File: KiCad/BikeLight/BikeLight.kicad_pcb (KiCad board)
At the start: 2 copper layers, 170.5 x 50 mm, 64 parts, among them J1 Conn-01x02_P2.5mm_S2B-XH-A-BK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, J2 Conn-01x02_P2.5mm_S2B-XH-A-BK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, J3 GT-USB-7051A, J4 Conn-01x02_P2.5mm_S2B-XH-A-BK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, J5 Conn-01x02_P2.5mm_S2B-XH-A-BK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, J6 Conn_01x05, Q1 AO3401A, Q2 AO3400A, Q3 BC847BDW1, SW2 SW_PB_B3F-4055, SW3 K2-1102AQ-H4CW-01, U1 TP4056-42-ESOP8, U2 MPU-6050, U3 MAX17048, U4 MCP1826S-33, U5 RFID-RC522, U6 MT3608, U8 HT-CT62

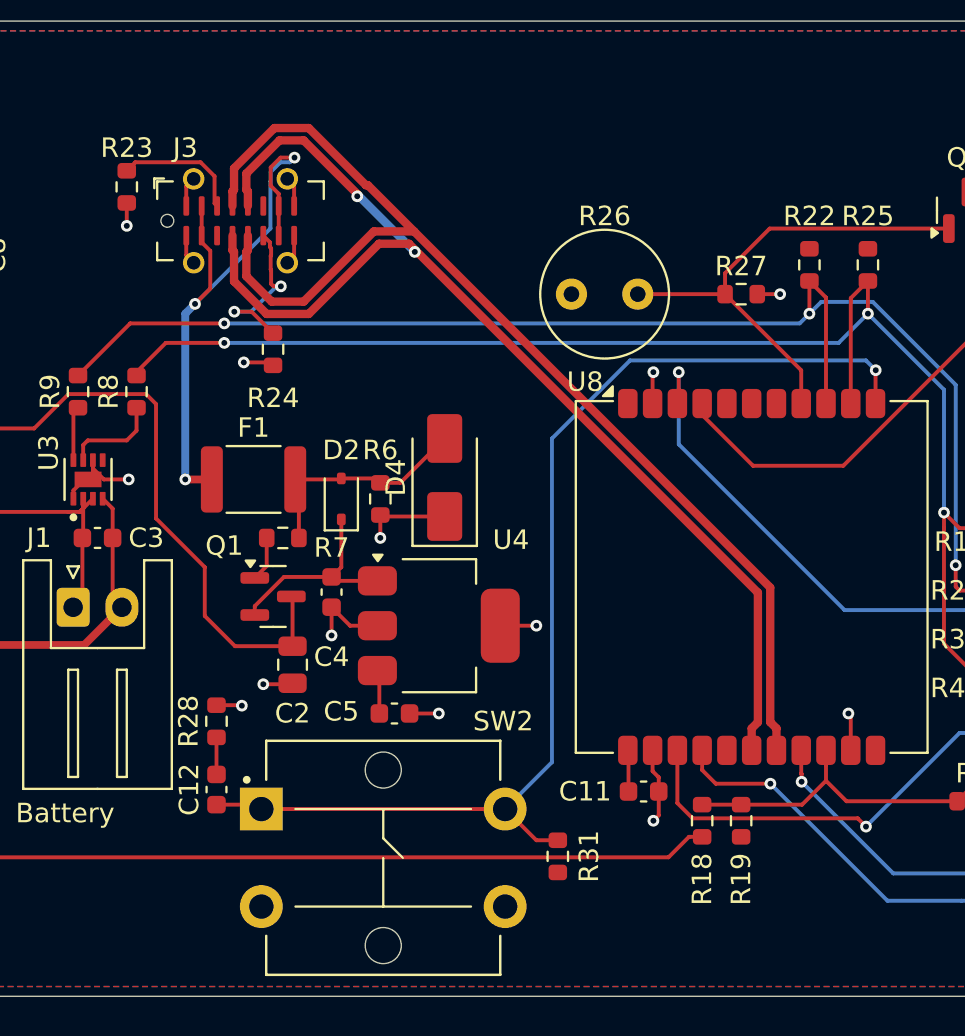
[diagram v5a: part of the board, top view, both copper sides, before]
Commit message: Changed and updated 3D models of devices
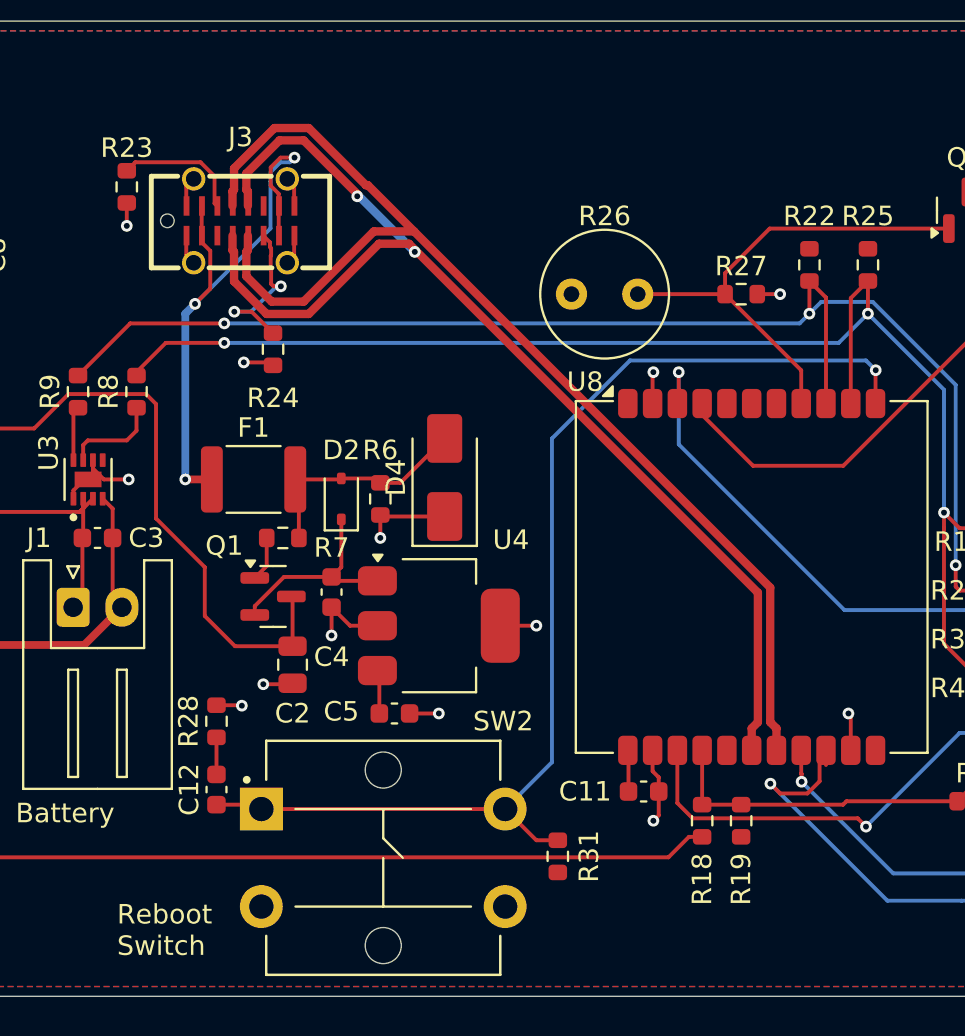
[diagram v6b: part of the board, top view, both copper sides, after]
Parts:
- J3: footprint Connector_USB:USB_C_Receptacle_G-Switch_GT-USB-7051x -> JLC2KICAD_Library:USB-C-SMD_GT-USB-7051A
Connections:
- U8 pad 15: /LED -> /IRQ
- U8 pad 17: /USB_DN -> /USB_DP
- U8 pad 18: /USB_DP -> /USB_DN
- U8 pad 20: /IRQ -> /LED
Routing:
- net /LED: track 80.7 -> 81.3 mm
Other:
- board text added: "Reboot Switch"

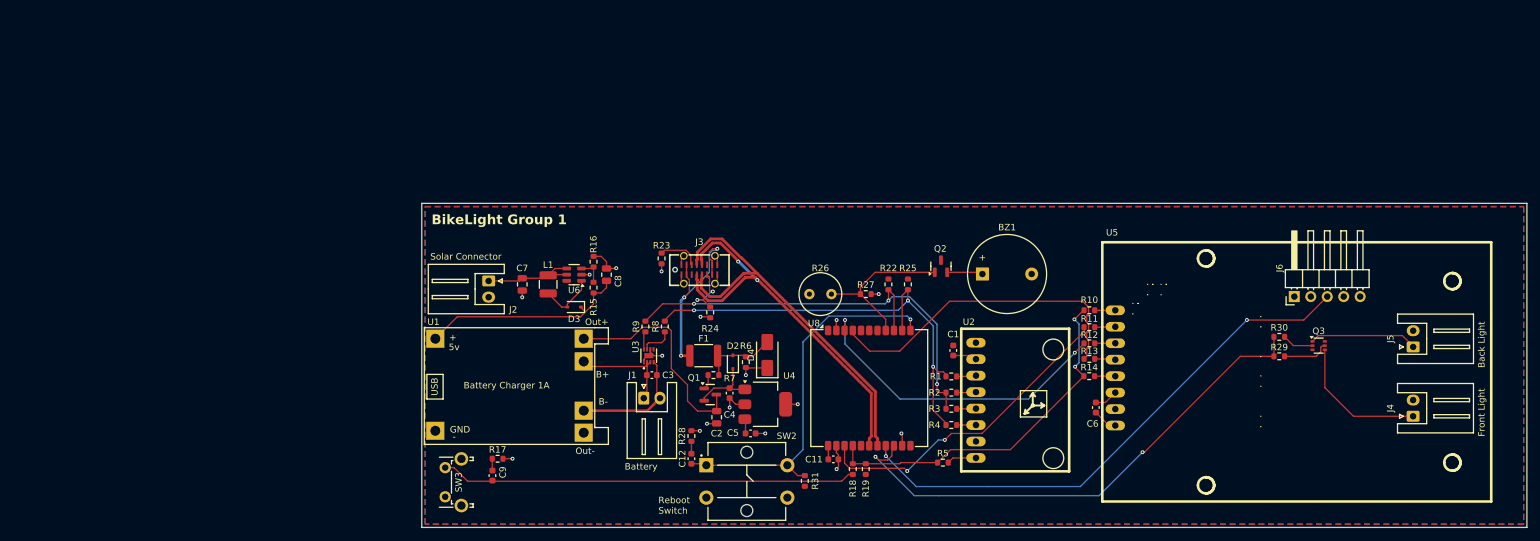
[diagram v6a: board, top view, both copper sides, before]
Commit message: changed sheet size
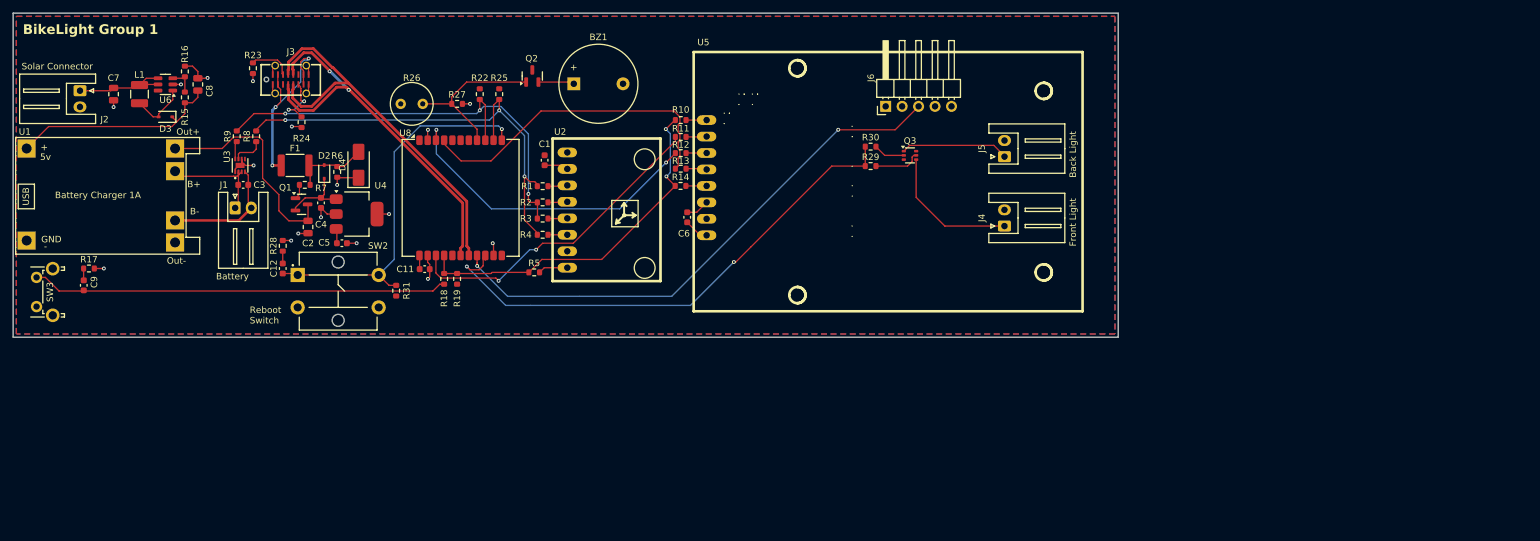
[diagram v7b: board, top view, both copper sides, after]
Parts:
- moved R17 69.5 mm to (33.1, 70.0)
- moved BZ1 69.5 mm to (108.0, 41.5)
- moved C12 69.5 mm to (63.0, 70.0)
- moved C4 69.5 mm to (69.0, 59.9)
- moved C6 69.5 mm to (125.4, 62.1)
- moved C9 69.5 mm to (32.4, 72.7)
- moved D4 69.5 mm to (74.8, 54.0)
- moved J1 69.5 mm to (55.7, 60.7)
- moved J5 69.5 mm to (174.4, 52.8)
- moved J6 69.5 mm to (156.1, 45.0)
- moved Q3 69.5 mm to (159.8, 52.6)
- moved R10 69.5 mm to (124.4, 47.1)
- moved R13 69.5 mm to (124.4, 54.6)
- moved R26 69.5 mm to (81.2, 44.6)
- moved R28 69.5 mm to (63.0, 66.5)
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
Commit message: Cleanup and created new fabrication files
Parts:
- moved C11 2.31 mm to (83.0, 69.0)
- moved C5 2.31 mm to (70.2, 65.0)
- moved C9 2.31 mm to (30.4, 71.5)
- moved R14 2.31 mm to (122.4, 56.2)
- moved R18 2.31 mm to (86.0, 70.5)
- moved R19 2.31 mm to (88.0, 70.5)
- moved R5 2.31 mm to (99.8, 69.5)
- moved U2 2.31 mm to (103.2, 70.8)
- moved BZ1 2.31 mm to (106.0, 40.4)
- moved C1 2.31 mm to (101.5, 52.2)
- moved C2 2.31 mm to (65.0, 62.5)
- moved C3 2.31 mm to (55.0, 56.0)
- moved C4 2.31 mm to (67.0, 58.8)
- moved C6 2.31 mm to (123.4, 61.0)
- moved C7 2.31 mm to (35.0, 42.0)
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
